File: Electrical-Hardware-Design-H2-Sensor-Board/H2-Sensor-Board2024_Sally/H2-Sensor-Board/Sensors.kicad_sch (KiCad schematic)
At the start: 28 parts, among them J4 Conn_01x03, J5 Conn_01x03, J6 Conn_01x03, J7 Conn_01x03, SW2 TARE BUTTON, U8 AD8608ARZ, U9 BME280

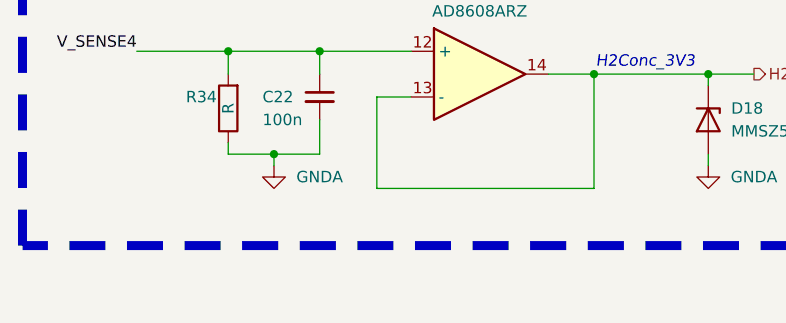
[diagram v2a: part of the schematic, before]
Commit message: updated pinout
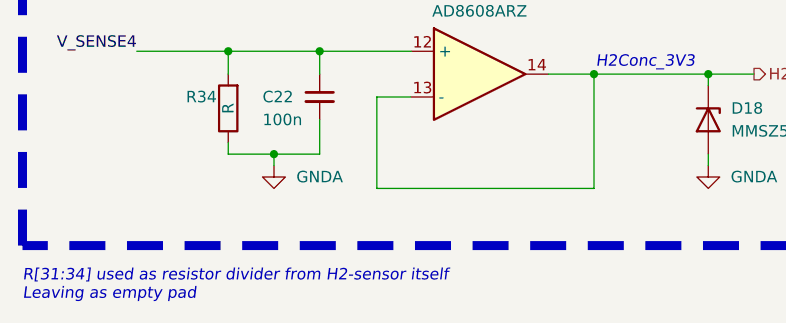
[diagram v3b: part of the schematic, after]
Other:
- note added: "R[31:34] used as resistor divider from H2-sensor itself Leaving as empty pad"
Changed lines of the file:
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@@
 		)
 	)
+	(text "R[31:34] used as resistor divider from H2-sensor itself\nLeaving as empty pad"
+		(exclude_from_sim no)
+		(at 15.24 139.7 0)
+		(effects
+			(font
+				(size 1.27 1.27)
+				(italic yes)
+				(color 0 0 255 1)
+			)
+			(justify left)
+		)
+	)
 	(text "H2Conc_3V3"
 		(exclude_from_sim no)
@@
 		(on_board yes)
 		(dnp no)
-		(property "Reference" "#PWR039"
+		(property "Reference" "#PWR040"
 			(at 121.285 115.57 0)
 			(effects
@@
 			(project "H2 Sensor Board Lucy Rev 1"
 				(path "/61fdd4a1-2d1e-44dc-8644-252e12d35745/7173564b-4ce8-4fe4-9cf3-378e96487dfe"
-					(reference "#PWR039")
+					(reference "#PWR040")
 					(unit 1)
 				)
@@
 		(on_board yes)
 		(dnp no)
-		(property "Reference" "#PWR030"
+		(property "Reference" "#PWR031"
 			(at 43.18 51.435 0)
 			(effects
@@
 			(project "H2 Sensor Board Lucy Rev 1"
 				(path "/61fdd4a1-2d1e-44dc-8644-252e12d35745/7173564b-4ce8-4fe4-9cf3-378e96487dfe"
-					(reference "#PWR030")
+					(reference "#PWR031")
 					(unit 1)
 				)
@@
 		(on_board yes)
 		(dnp no)
-		(property "Reference" "#PWR034"
+		(property "Reference" "#PWR035"
 			(at 91.44 51.435 0)
 			(effects
@@
 			(project "H2 Sensor Board Lucy Rev 1"
 				(path "/61fdd4a1-2d1e-44dc-8644-252e12d35745/7173564b-4ce8-4fe4-9cf3-378e96487dfe"
-					(reference "#PWR034")
+					(reference "#PWR035")
 					(unit 1)
 				)
@@
 		(on_board yes)
 		(dnp no)
-		(property "Reference" "#PWR046"
+		(property "Reference" "#PWR047"
 			(at 170.815 113.665 0)
 			(effects
@@
 			(project "H2-Sensor-Board_Sally-R1.0"
 				(path "/61fdd4a1-2d1e-44dc-8644-252e12d35745/7173564b-4ce8-4fe4-9cf3-378e96487dfe"
-					(reference "#PWR046")
+					(reference "#PWR047")
 					(unit 1)
 				)
@@
 		(on_board yes)
 		(dnp no)
-		(property "Reference" "#PWR031"
+		(property "Reference" "#PWR032"
 			(at 43.18 79.375 0)
 			(effects
@@
 			(project "H2-Sensor-Board_Sally-R1.0"
 				(path "/61fdd4a1-2d1e-44dc-8644-252e12d35745/7173564b-4ce8-4fe4-9cf3-378e96487dfe"
-					(reference "#PWR031")
+					(reference "#PWR032")
 					(unit 1)
 				)
@@
 		(on_board yes)
 		(dnp no)
-		(property "Reference" "#PWR036"
+		(property "Reference" "#PWR037"
 			(at 91.44 106.045 0)
 			(effects
@@
 			(project "H2-Sensor-Board_Sally-R1.0"
 				(path "/61fdd4a1-2d1e-44dc-8644-252e12d35745/7173564b-4ce8-4fe4-9cf3-378e96487dfe"
-					(reference "#PWR036")
+					(reference "#PWR037")
 					(unit 1)
 				)
@@
 		(on_board yes)
 		(dnp no)
-		(property "Reference" "#PWR033"
+		(property "Reference" "#PWR034"
 			(at 43.18 132.715 0)
 			(effects
@@
 			(project "H2-Sensor-Board_Sally-R1.0"
 				(path "/61fdd4a1-2d1e-44dc-8644-252e12d35745/7173564b-4ce8-4fe4-9cf3-378e96487dfe"
-					(reference "#PWR033")
+					(reference "#PWR034")
 					(unit 1)
 				)
@@
 		(dnp no)
 		(fields_autoplaced yes)
-		(property "Reference" "#PWR049"
+		(property "Reference" "#PWR050"
 			(at 184.785 76.2 0)
 			(effects
@@
 			(project "H2 Sensor Board Lucy Rev 1"
 				(path "/61fdd4a1-2d1e-44dc-8644-252e12d35745/7173564b-4ce8-4fe4-9cf3-378e96487dfe"
-					(reference "#PWR049")
+					(reference "#PWR050")
 					(unit 1)
 				)
@@
 		(dnp no)
 		(fields_autoplaced yes)
-		(property "Reference" "#PWR051"
+		(property "Reference" "#PWR052"
 			(at 241.935 36.83 0)
 			(effects
@@
 			(project "H2 Sensor Board Lucy Rev 1"
 				(path "/61fdd4a1-2d1e-44dc-8644-252e12d35745/7173564b-4ce8-4fe4-9cf3-378e96487dfe"
-					(reference "#PWR051")
+					(reference "#PWR052")
 					(unit 1)
 				)
@@
 		(dnp no)
 		(fields_autoplaced yes)
-		(property "Reference" "#PWR048"
+		(property "Reference" "#PWR049"
 			(at 182.245 29.21 0)
 			(effects
@@
 			(project "H2 Sensor Board Lucy Rev 1"
 				(path "/61fdd4a1-2d1e-44dc-8644-252e12d35745/7173564b-4ce8-4fe4-9cf3-378e96487dfe"
-					(reference "#PWR048")
+					(reference "#PWR049")
 					(unit 1)
 				)
@@
 		(on_board yes)
 		(dnp no)
-		(property "Reference" "#PWR035"
+		(property "Reference" "#PWR036"
 			(at 91.44 79.375 0)
 			(effects
@@
 			(project "H2-Sensor-Board_Sally-R1.0"
 				(path "/61fdd4a1-2d1e-44dc-8644-252e12d35745/7173564b-4ce8-4fe4-9cf3-378e96487dfe"
-					(reference "#PWR035")
+					(reference "#PWR036")
 					(unit 1)
 				)
@@
 		(on_board yes)
 		(dnp no)
-		(property "Reference" "#PWR040"
+		(property "Reference" "#PWR041"
 			(at 128.27 39.37 0)
 			(effects
@@
 			(project ""
 				(path "/61fdd4a1-2d1e-44dc-8644-252e12d35745/7173564b-4ce8-4fe4-9cf3-378e96487dfe"
-					(reference "#PWR040")
+					(reference "#PWR041")
 					(unit 1)
 				)
@@
 		(on_board yes)
 		(dnp no)
-		(property "Reference" "#PWR037"
+		(property "Reference" "#PWR038"
 			(at 91.44 132.715 0)
 			(effects
@@
 			(project "H2-Sensor-Board_Sally-R1.0"
 				(path "/61fdd4a1-2d1e-44dc-8644-252e12d35745/7173564b-4ce8-4fe4-9cf3-378e96487dfe"
-					(reference "#PWR037")
+					(reference "#PWR038")
 					(unit 1)
 				)
@@
 		(on_board yes)
 		(dnp no)
-		(property "Reference" "#PWR052"
+		(property "Reference" "#PWR053"
 			(at 262.255 33.02 0)
 			(effects
@@
 			(project "H2 Sensor Board Lucy Rev 1"
 				(path "/61fdd4a1-2d1e-44dc-8644-252e12d35745/7173564b-4ce8-4fe4-9cf3-378e96487dfe"
-					(reference "#PWR052")
+					(reference "#PWR053")
 					(unit 1)
 				)
@@
 		(on_board yes)
 		(dnp no)
-		(property "Reference" "#PWR032"
+		(property "Reference" "#PWR033"
 			(at 43.18 106.045 0)
 			(effects
@@
 			(project "H2-Sensor-Board_Sally-R1.0"
 				(path "/61fdd4a1-2d1e-44dc-8644-252e12d35745/7173564b-4ce8-4fe4-9cf3-378e96487dfe"
-					(reference "#PWR032")
+					(reference "#PWR033")
 					(unit 1)
 				)
@@
 			(project "H2 Sensor Board Lucy Rev 1"
 				(path "/61fdd4a1-2d1e-44dc-8644-252e12d35745/7173564b-4ce8-4fe4-9cf3-378e96487dfe"
-					(reference "#PWR038")
+					(reference "#PWR039")
 					(unit 1)
 				)
@@
 		(dnp no)
 		(fields_autoplaced yes)
-		(property "Reference" "#PWR053"
+		(property "Reference" "#PWR054"
 			(at 269.875 22.86 0)
 			(effects
@@
 			(project "H2 Sensor Board Lucy Rev 1"
 				(path "/61fdd4a1-2d1e-44dc-8644-252e12d35745/7173564b-4ce8-4fe4-9cf3-378e96487dfe"
-					(reference "#PWR053")
+					(reference "#PWR054")
 					(unit 1)
 				)
@@
 		(on_board yes)
 		(dnp no)
-		(property "Reference" "#PWR044"
+		(property "Reference" "#PWR045"
 			(at 170.815 88.265 0)
 			(effects
@@
 			(project "H2 Sensor Board Lucy Rev 1"
 				(path "/61fdd4a1-2d1e-44dc-8644-252e12d35745/7173564b-4ce8-4fe4-9cf3-378e96487dfe"
-					(reference "#PWR044")
+					(reference "#PWR045")
 					(unit 1)
 				)
@@
 			(project "H2 Sensor Board Lucy Rev 1"
 				(path "/61fdd4a1-2d1e-44dc-8644-252e12d35745/7173564b-4ce8-4fe4-9cf3-378e96487dfe"
-					(reference "#PWR042")
+					(reference "#PWR043")
 					(unit 1)
 				)
@@
 		(dnp no)
 		(fields_autoplaced yes)
-		(property "Reference" "#PWR043"
+		(property "Reference" "#PWR044"
 			(at 163.195 43.18 0)
 			(effects
@@
 			(project "H2 Sensor Board Lucy Rev 1"
 				(path "/61fdd4a1-2d1e-44dc-8644-252e12d35745/7173564b-4ce8-4fe4-9cf3-378e96487dfe"
-					(reference "#PWR043")
+					(reference "#PWR044")
 					(unit 1)
 				)
@@
 		(dnp no)
 		(fields_autoplaced yes)
-		(property "Reference" "#PWR050"
+		(property "Reference" "#PWR051"
 			(at 208.915 43.18 0)
 			(effects
@@
 			(project "H2 Sensor Board Lucy Rev 1"
 				(path "/61fdd4a1-2d1e-44dc-8644-252e12d35745/7173564b-4ce8-4fe4-9cf3-378e96487dfe"
-					(reference "#PWR050")
+					(reference "#PWR051")
 					(unit 1)
 				)
@@
 		(on_board yes)
 		(dnp no)
-		(property "Reference" "#PWR041"
+		(property "Reference" "#PWR042"
 			(at 128.27 65.405 0)
 			(effects
@@
 			(project ""
 				(path "/61fdd4a1-2d1e-44dc-8644-252e12d35745/7173564b-4ce8-4fe4-9cf3-378e96487dfe"
-					(reference "#PWR041")
+					(reference "#PWR042")
 					(unit 1)
 				)
@@
 		(on_board yes)
 		(dnp no)
-		(property "Reference" "#PWR047"
+		(property "Reference" "#PWR048"
 			(at 170.815 126.365 0)
 			(effects
@@
 			(project "H2-Sensor-Board_Sally-R1.0"
 				(path "/61fdd4a1-2d1e-44dc-8644-252e12d35745/7173564b-4ce8-4fe4-9cf3-378e96487dfe"
-					(reference "#PWR047")
+					(reference "#PWR048")
 					(unit 1)
 				)
@@
 		(on_board yes)
 		(dnp no)
-		(property "Reference" "#PWR045"
+		(property "Reference" "#PWR046"
 			(at 170.815 100.965 0)
 			(effects
@@
 			(project "H2-Sensor-Board_Sally-R1.0"
 				(path "/61fdd4a1-2d1e-44dc-8644-252e12d35745/7173564b-4ce8-4fe4-9cf3-378e96487dfe"
-					(reference "#PWR045")
+					(reference "#PWR046")
 					(unit 1)
 				)

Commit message: lots of work
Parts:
- removed J4, J5, J6, J7: Conn_01x03, ecocad_lib_footprints:TE_1-770967-0, symbol Connector_Generic:Conn_01x03
- removed NT1: NetTie_2, NetTie:NetTie-2_SMD_Pad2.0mm, symbol Device:NetTie_2
- added J4, J5, J6, J7: Molex_6_Pin, ecocad_lib_footprints:Molex_6_Pin_FTP, symbol ecocad_lib_symbols:Molex_6_Pin
- renumbered C19 to C23, C20 to C24, C21 to C25, C22 to C26, C23 to C27, C25 to C29, C26 to C30, D15 to D17, D16 to D18, D17 to D19, D18 to D20, R31 to R33, R32 to R34, R33 to R35, R34 to R36, R35 to R37, R36 to R38
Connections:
- net GNDA is gone; now on net GND: C23.2, C24.2, C25.2, C26.2, C27.2, D17.2 (A), D18.2 (A), D19.2 (A), D20.2 (A), R33.1, R34.1, R35.1, R36.1, U8.11 (V-)
- net GND: now also J4.1, J4.4, J5.1, J5.4, J6.1, J6.4, J7.1, J7.4
- net V_HEAT: now also J4.2, J4.5, J5.2, J5.5, J6.2, J6.5, J7.2, J7.5
- net V_SENSE1: now also J4.3, J4.6
- net V_SENSE2: now also J5.3, J5.6
- net V_SENSE3: now also J6.3, J6.6
- net V_SENSE4: now also J7.3, J7.6

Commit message: changes
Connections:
- net +5V: now also U8.8 (V+); no longer U8.4 (V+)
- net GND: now also U8.4 (V-); no longer U8.11 (V-)
- net H2_CONC2: now also U8.1, U8.2 (-); no longer U8.6 (-), U8.7
- net H2_CONC3: now also U8.1, U8.2 (-); no longer U8.8, U8.9 (-)
- net H2_CONC4: now also U8.1, U8.2 (-); no longer U8.13 (-), U8.14
- net V_SENSE2: now also U8.3 (+); no longer U8.5 (+)
- net V_SENSE3: now also U8.3 (+); no longer U8.10 (+)
- net V_SENSE4: now also U8.3 (+); no longer U8.12 (+)
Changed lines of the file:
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@@
 			)
 		)
-		(pin "12"
+		(pin "1"
 		)
-		(pin "11"
+		(pin "2"
 		)
 		(pin "3"
 		)
-		(pin "7"
+		(pin "1"
 		)
-		(pin "6"
+		(pin "2"
 		)
-		(pin "9"
+		(pin "2"
 		)
 		(pin "1"
 		)
-		(pin "5"
+		(pin "3"
 		)
-		(pin "10"
+		(pin "3"
 		)
-		(pin "13"
+		(pin "3"
 		)
 		(pin "8"
 		)
-		(pin "14"
+		(pin "1"
 		)
 		(pin "4"
@@
 			)
 		)
-		(pin "12"
+		(pin "2"
 		)
-		(pin "11"
+		(pin "1"
 		)
 		(pin "3"
 		)
-		(pin "7"
+		(pin "3"
 		)
-		(pin "6"
+		(pin "1"
 		)
-		(pin "9"
+		(pin "2"
 		)
 		(pin "1"
 		)
-		(pin "5"
+		(pin "3"
 		)
-		(pin "10"
+		(pin "3"
 		)
-		(pin "13"
+		(pin "2"
 		)
 		(pin "8"
 		)
-		(pin "14"
+		(pin "1"
 		)
 		(pin "4"
@@
 			)
 		)
-		(pin "12"
+		(pin "2"
 		)
-		(pin "11"
+		(pin "2"
 		)
 		(pin "3"
 		)
-		(pin "7"
+		(pin "3"
 		)
-		(pin "6"
+		(pin "1"
 		)
-		(pin "9"
+		(pin "3"
 		)
 		(pin "1"
 		)
-		(pin "5"
+		(pin "2"
 		)
-		(pin "10"
+		(pin "3"
 		)
-		(pin "13"
+		(pin "1"
 		)
 		(pin "8"
 		)
-		(pin "14"
+		(pin "1"
 		)
 		(pin "4"
@@
 			)
 		)
-		(pin "7"
+		(pin "2"
 		)
-		(pin "5"
+		(pin "3"
 		)
 		(pin "2"
@@
 		(pin "1"
 		)
-		(pin "9"
+		(pin "1"
 		)
-		(pin "13"
+		(pin "3"
 		)
-		(pin "14"
+		(pin "3"
 		)
-		(pin "10"
+		(pin "2"
 		)
 		(pin "3"
@@
 		(pin "4"
 		)
-		(pin "11"
+		(pin "1"
 		)
-		(pin "6"
+		(pin "2"
 		)
-		(pin "12"
+		(pin "1"
 		)
 		(instances
@@
 			)
 		)
-		(pin "12"
+		(pin "2"
 		)
-		(pin "11"
+		(pin "1"
 		)
 		(pin "3"
 		)
-		(pin "7"
+		(pin "2"
 		)
-		(pin "6"
+		(pin "3"
 		)
-		(pin "9"
+		(pin "1"
 		)
 		(pin "1"
 		)
-		(pin "5"
+		(pin "2"
 		)
-		(pin "10"
+		(pin "3"
 		)
-		(pin "13"
+		(pin "1"
 		)
 		(pin "8"
 		)
-		(pin "14"
+		(pin "3"
 		)
 		(pin "4"

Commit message: end-of-day update
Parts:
- renumbered J4 to J3, J5 to J4, J6 to J5, J7 to J6
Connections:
- net +5V: now also U8.4 (V+); no longer U8.8 (V+)
- net GND: now also U8.11 (V-); no longer U8.4 (V-)
- net H2_CONC2: now also U8.6 (-), U8.7; no longer U8.1, U8.2 (-)
- net H2_CONC3: now also U8.8, U8.9 (-); no longer U8.1, U8.2 (-)
- net H2_CONC4: now also U8.13 (-), U8.14; no longer U8.1, U8.2 (-)
- net V_SENSE2: now also U8.5 (+); no longer U8.3 (+)
- net V_SENSE3: now also U8.10 (+); no longer U8.3 (+)
- net V_SENSE4: now also U8.12 (+); no longer U8.3 (+)

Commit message: A
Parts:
- R33, R34, R35, R36: value R -> 4k7
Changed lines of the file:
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@@
 			)
 		)
-		(property "Value" "R"
+		(property "Value" "4k7"
 			(at 38.1 120.015 90)
 			(effects
@@
 			)
 		)
-		(property "Value" "R"
+		(property "Value" "4k7"
 			(at 38.1 66.675 90)
 			(effects
@@
 			)
 		)
-		(property "Value" "R"
+		(property "Value" "4k7"
 			(at 38.1 38.735 90)
 			(effects
@@
 			)
 		)
-		(property "Value" "R"
+		(property "Value" "4k7"
 			(at 38.1 93.345 90)
 			(effects
